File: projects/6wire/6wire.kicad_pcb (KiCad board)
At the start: 2 copper layers, 30 x 34 mm, 58 parts, among them J1 USB_B_Micro, J2 guard, J3 4wire, J4 SWD/UART, Q1 DMP3099L, Q2 DMP3099L, SW1 BUT, U1 AZ1117-3.3, U2 ATSAMD21G16B-M, U3 ADS122C04, U4 MCP6L02x-xMS, U5 MAX4639EUE, U6 MAX4238AUT, Y1 32.768kHz

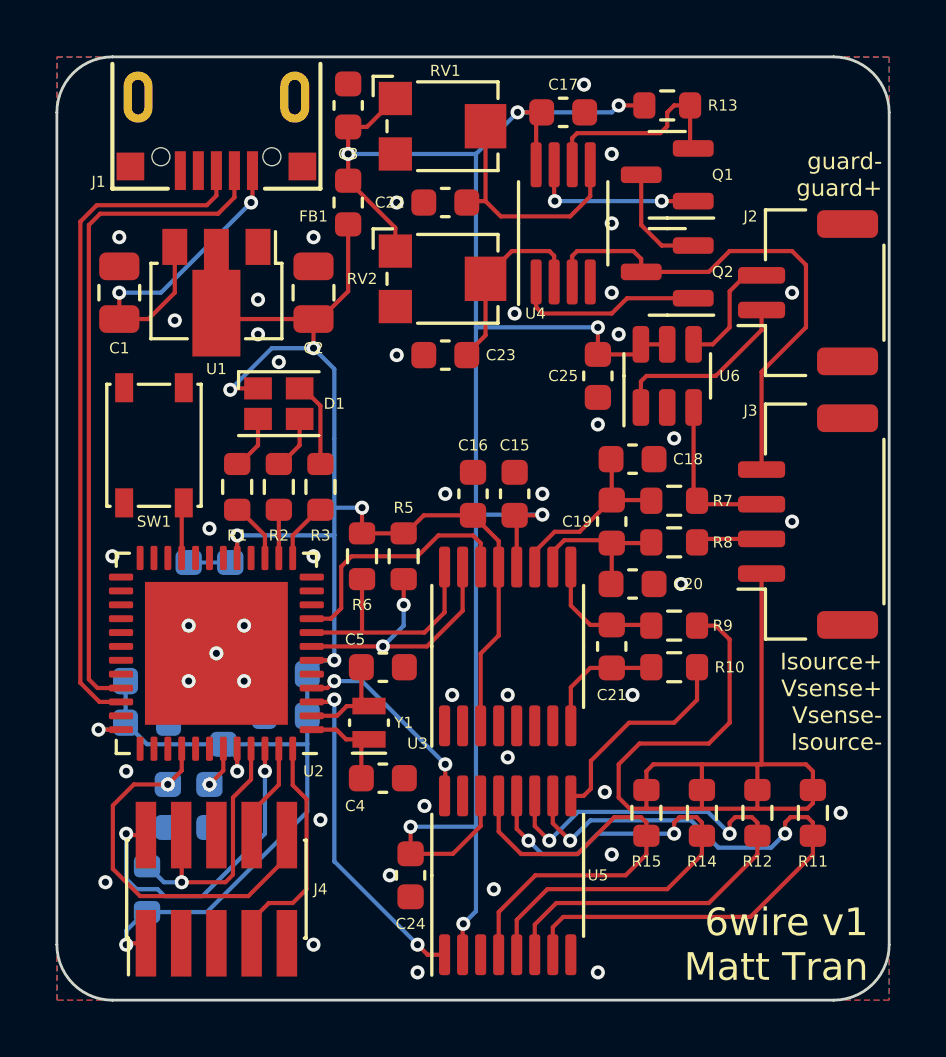
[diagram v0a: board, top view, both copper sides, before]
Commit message: update 6wire to v1.1
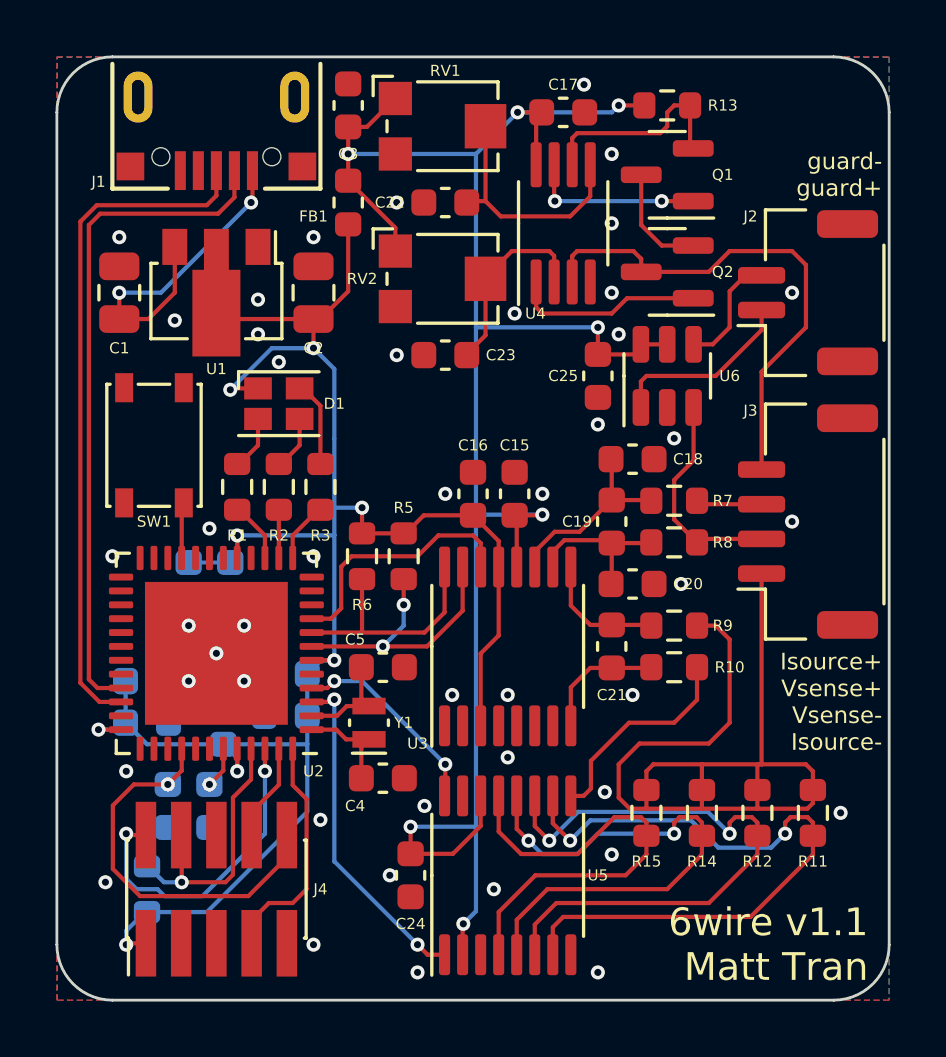
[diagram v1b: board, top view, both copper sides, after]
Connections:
- U6 pad 3: /4wire/Vsense+ -> /4wire/Vsense-
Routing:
- net /4wire/Vsense-: track 2.38 -> 7.87 mm
- net /4wire/Vsense+: track 5.79 -> 2.38 mm
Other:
- board text added: "6wire v1.1 Matt Tran"
- board text removed: "6wire v1 Matt Tran"
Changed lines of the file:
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@@
       (net 1 "GND") (pinfunction "V-") (pintype "power_in"))
     (pad "3" smd roundrect locked (at -1.1375 0.95 90) (size 1.325 0.6) (layers "F.Cu" "F.Paste" "F.Mask") (roundrect_rratio 0.25)
-      (net 24 "/4wire/Vsense+") (pinfunction "+") (pintype "input"))
+      (net 25 "/4wire/Vsense-") (pinfunction "+") (pintype "input"))
     (pad "4" smd roundrect locked (at 1.1375 0.95 90) (size 1.325 0.6) (layers "F.Cu" "F.Paste" "F.Mask") (roundrect_rratio 0.25)
       (net 22 "/guard/guard-") (pinfunction "-") (pintype "input"))
@@
   (gr_line (start 144.25 110.5) (end 144.25 80.5) (layer "Edge.Cuts") (width 0.1))
   (gr_arc (start 174.25 110.5) (mid 173.664214 111.914214) (end 172.25 112.5) (layer "Edge.Cuts") (width 0.1))
-  (gr_text "6wire v1\nMatt Tran" (at 173.5 110.5) (layer "F.SilkS")
+  (gr_text "6wire v1.1\nMatt Tran" (at 173.5 110.5) (layer "F.SilkS")
     (effects (font (size 1 1) (thickness 0.2)) (justify right))
   )
@@
   (segment (start 165.3125 85.78125) (end 165.3125 86.25) (width 0.1524) (layer "F.Cu") (net 23))
   (segment (start 165.3125 86.25) (end 167.75 86.25) (width 0.1524) (layer "F.Cu") (net 23))
-  (segment (start 167.2 91.1375) (end 167.2 94.375) (width 0.1524) (layer "F.Cu") (net 24))
   (segment (start 169.65 94.625) (end 167.45 94.625) (width 0.1524) (layer "F.Cu") (net 24))
   (segment (start 167.45 94.625) (end 167.325 94.5) (width 0.1524) (layer "F.Cu") (net 24))
-  (segment (start 167.2 94.375) (end 167.325 94.5) (width 0.1524) (layer "F.Cu") (net 24))
+  (segment (start 167.2 91.1375) (end 167.2 93.05) (width 0.1524) (layer "F.Cu") (net 25))
+  (segment (start 166.5 93.75) (end 166.5 95.175) (width 0.1524) (layer "F.Cu") (net 25))
+  (segment (start 167.2 93.05) (end 166.5 93.75) (width 0.1524) (layer "F.Cu") (net 25))
   (segment (start 167.45 95.875) (end 167.325 96) (width 0.1524) (layer "F.Cu") (net 25))
   (segment (start 169.65 95.875) (end 167.45 95.875) (width 0.1524) (layer "F.Cu") (net 25))
+  (segment (start 166.5 95.175) (end 167.325 96) (width 0.1524) (layer "F.Cu") (net 25))
   (segment (start 167.325 99) (end 168 99) (width 0.1524) (layer "F.Cu") (net 26))
   (segment (start 168.5 99.5) (end 168.5 102.5) (width 0.1524) (layer "F.Cu") (net 26))
